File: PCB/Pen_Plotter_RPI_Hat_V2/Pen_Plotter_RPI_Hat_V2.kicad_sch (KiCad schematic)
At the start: 3 parts, among them J1 RASM712PX, U2 MINI560, U9 ATmega328P-P

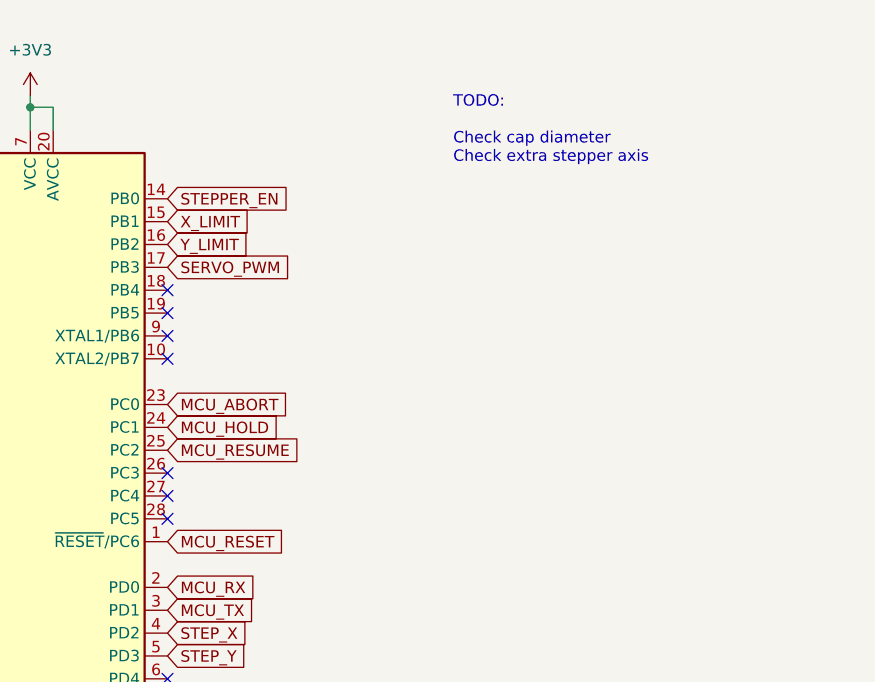
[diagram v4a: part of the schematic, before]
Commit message: Completed PCB layout
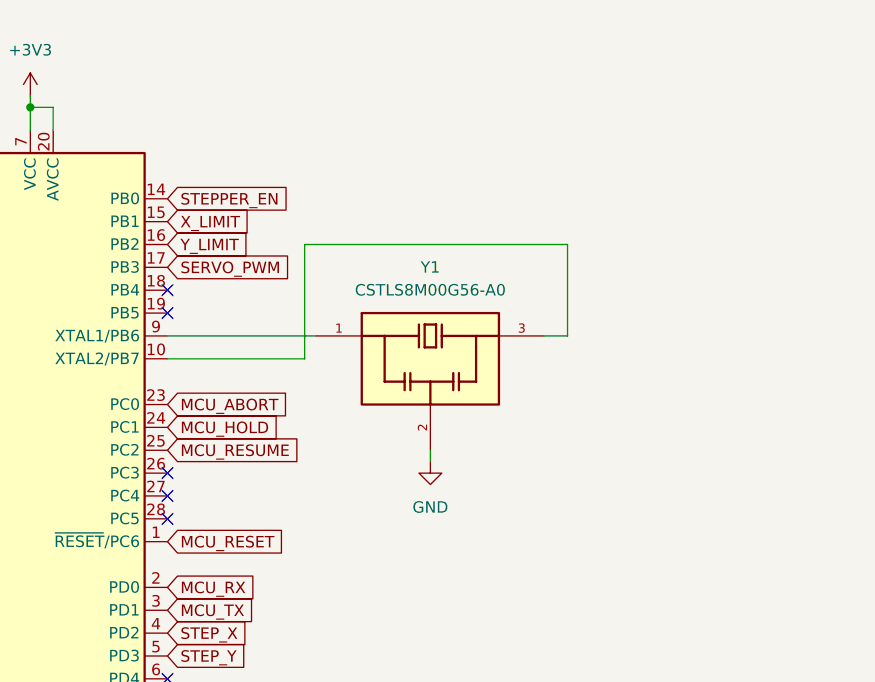
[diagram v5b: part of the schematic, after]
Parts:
- added Y1: CSTLS8M00G56-A0, Pen_Plotter_Lib:OSC_CSTLS8M00G56-A0, symbol Pen_Plotter_Lib:CSTLS8M00G56-A0
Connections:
- net GND: now also Y1.2
- net at U9.10 (XTAL2/PB7): now also Y1.3
- net at U9.9 (XTAL1/PB6): now also Y1.1
- no-connect marks 9 -> 7
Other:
- note removed: "TODO: Check cap diameter Check extra stepper axis"
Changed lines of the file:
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@@
   (junction (at 48.26 29.21) (diameter 0) (color 0 0 0 0)
   )
-  (no_connect (at 63.5 54.61))
   (no_connect (at 63.5 74.93))
   (no_connect (at 63.5 72.39))
@@
   (no_connect (at 63.5 69.85))
   (no_connect (at 63.5 49.53))
-  (no_connect (at 63.5 57.15))
   (no_connect (at 63.5 100.33))
   (wire (pts (xy 254 50.8) (xy 257.81 50.8))
@@
     (stroke (width 0) (type default))
   )
+  (wire (pts (xy 63.5 54.61) (xy 80.01 54.61))
+    (stroke (width 0) (type default))
+  )
   (wire (pts (xy 224.79 63.5) (xy 224.79 50.8))
     (stroke (width 0) (type default))
@@
     (stroke (width 0) (type default))
   )
+  (wire (pts (xy 107.95 44.45) (xy 107.95 54.61))
+    (stroke (width 0) (type default))
+  )
+  (wire (pts (xy 107.95 54.61) (xy 105.41 54.61))
+    (stroke (width 0) (type default))
+  )
   (wire (pts (xy 257.81 38.1) (xy 257.81 40.64))
     (stroke (width 0) (type default))
@@
     (stroke (width 0) (type default))
   )
+  (wire (pts (xy 92.71 67.31) (xy 92.71 68.58))
+    (stroke (width 0) (type default))
+  )
   (wire (pts (xy 30.48 39.37) (xy 30.48 43.18))
     (stroke (width 0) (type default))
@@
     (stroke (width 0) (type default))
   )
+  (wire (pts (xy 78.74 57.15) (xy 78.74 44.45))
+    (stroke (width 0) (type default))
+  )
   (wire (pts (xy 195.58 35.56) (xy 195.58 36.83))
     (stroke (width 0) (type default))
   )
+  (wire (pts (xy 63.5 57.15) (xy 78.74 57.15))
+    (stroke (width 0) (type default))
+  )
   (wire (pts (xy 48.26 107.95) (xy 48.26 109.22))
+    (stroke (width 0) (type default))
+  )
+  (wire (pts (xy 78.74 44.45) (xy 107.95 44.45))
     (stroke (width 0) (type default))
   )
@@
     (effects (font (size 1.27 1.27)) (justify left bottom))
   )
-  (text "TODO:\n\nCheck cap diameter\nCheck extra stepper axis"
-    (at 95.25 35.56 0)
-    (effects (font (size 1.27 1.27)) (justify left bottom))
-  )
   (text "BARREL_JACK_12V" (at 170.18 21.59 0)
     (effects (font (size 1.27 1.27)) (justify left bottom))
@@
         (path "/a2e71921-3692-4a11-8676-7b25cde44301"
           (reference "#PWR013") (unit 1)
+        )
+      )
+    )
+  )
+  (symbol (lib_id "Pen_Plotter_Lib:CSTLS8M00G56-A0") (at 92.71 57.15 0) (unit 1)
+    (in_bom yes) (on_board yes) (dnp no) (fields_autoplaced)
+    (property "Reference" "Y1" (at 92.71 46.99 0)
+      (effects (font (size 1.27 1.27)))
+    )
+    (property "Value" "CSTLS8M00G56-A0" (at 92.71 49.53 0)
+      (effects (font (size 1.27 1.27)))
+    )
+    (property "Footprint" "Pen_Plotter_Lib:OSC_CSTLS8M00G56-A0" (at 92.71 57.15 0)
+      (effects (font (size 1.27 1.27)) (justify bottom) hide)
+    )
+    (property "Datasheet" "" (at 92.71 57.15 0)
+      (effects (font (size 1.27 1.27)) hide)
+    )
+    (property "PARTREV" "March 23, 2017" (at 92.71 57.15 0)
+      (effects (font (size 1.27 1.27)) (justify bottom) hide)
+    )
+    (property "MANUFACTURER" "Murata" (at 92.71 57.15 0)
+      (effects (font (size 1.27 1.27)) (justify bottom) hide)
+    )
+    (property "MAXIMUM_PACKAGE_HEIGHT" "6.00mm" (at 92.71 57.15 0)
+      (effects (font (size 1.27 1.27)) (justify bottom) hide)
+    )
+    (property "STANDARD" "IPC-7351B" (at 92.71 57.15 0)
+      (effects (font (size 1.27 1.27)) (justify bottom) hide)
+    )
+    (pin "1")
+    (pin "2")
+    (pin "3")
+    (instances
+      (project "Pen_Plotter_RPI_Hat_V2"
+        (path "/a2e71921-3692-4a11-8676-7b25cde44301"
+          (reference "Y1") (unit 1)
         )
       )
@@
         )
       )
+    )
+  )
+  (symbol (lib_id "power:GND") (at 92.71 68.58 0) (unit 1)
+    (in_bom yes) (on_board yes) (dnp no) (fields_autoplaced)
+    (property "Reference" "#PWR012" (at 92.71 74.93 0)
+      (effects (font (size 1.27 1.27)) hide)
+    )
+    (property "Value" "GND" (at 92.71 73.66 0)
+      (effects (font (size 1.27 1.27)))
+    )
+    (property "Footprint" "" (at 92.71 68.58 0)
+      (effects (font (size 1.27 1.27)) hide)
+    )
+    (property "Datasheet" "" (at 92.71 68.58 0)
+      (effects (font (size 1.27 1.27)) hide)
+    )
+    (pin "1")
+    (instances
+      (project "Pen_Plotter_RPI_Hat_V2"
+        (path "/a2e71921-3692-4a11-8676-7b25cde44301"
+          (reference "#PWR012") (unit 1)
+        )
+      )
